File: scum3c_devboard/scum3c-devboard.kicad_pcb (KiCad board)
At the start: 2 copper layers, 142.2 x 96.5 mm, 59 parts, among them J1 47346-0001, J2 Conn_Coaxial, P3 Conn_01x02, P4 Conn_01x24, P5 Conn_01x02, U1 LP5907MFX-1.5, U10 LTC4123, U2 74AVC1T45GS,132, U3 FT231XS-U, U4 74AVC1T45GS,132, U5 74AVC4TD245PW,118, U6 74AVC4TD245PW,118, U7 ADT7302ARMZ, U8 scum3, U9AB1 MPU-9250

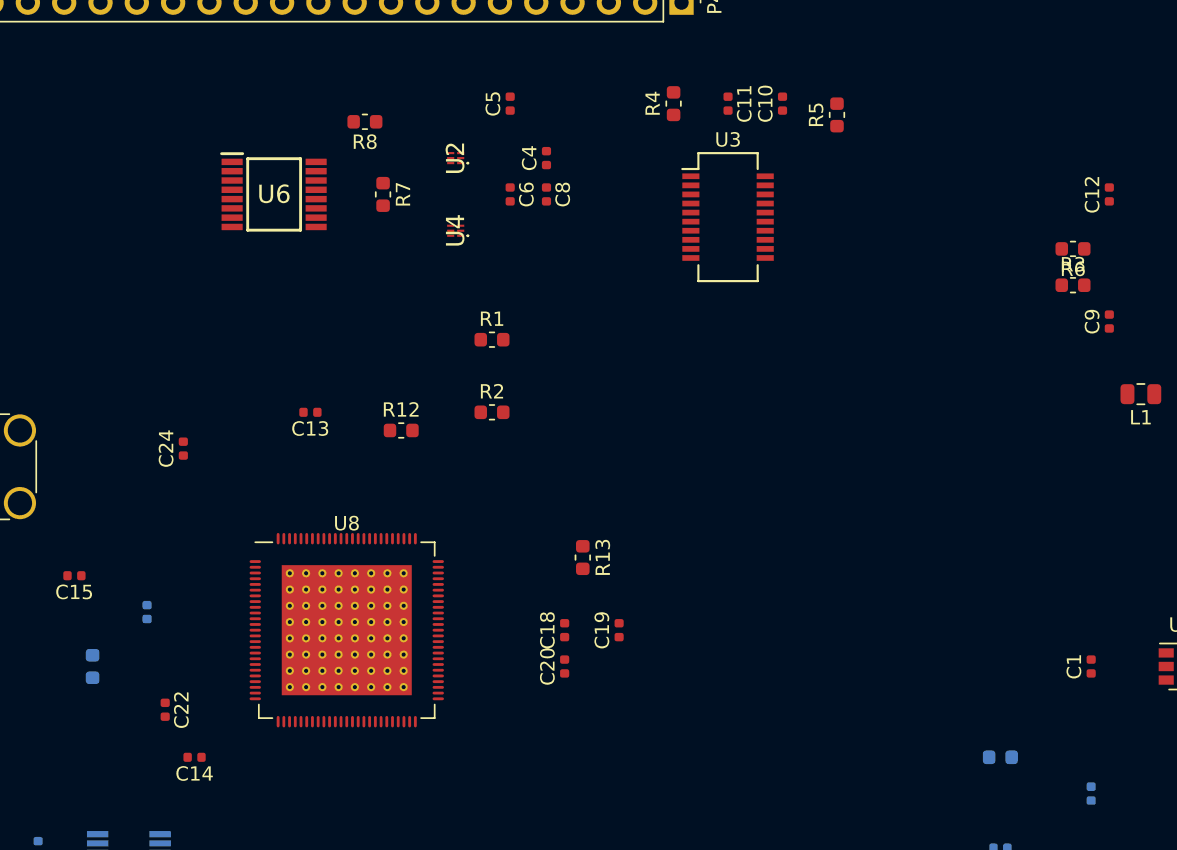
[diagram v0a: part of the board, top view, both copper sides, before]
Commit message: changed resistor smd footprint to 0402
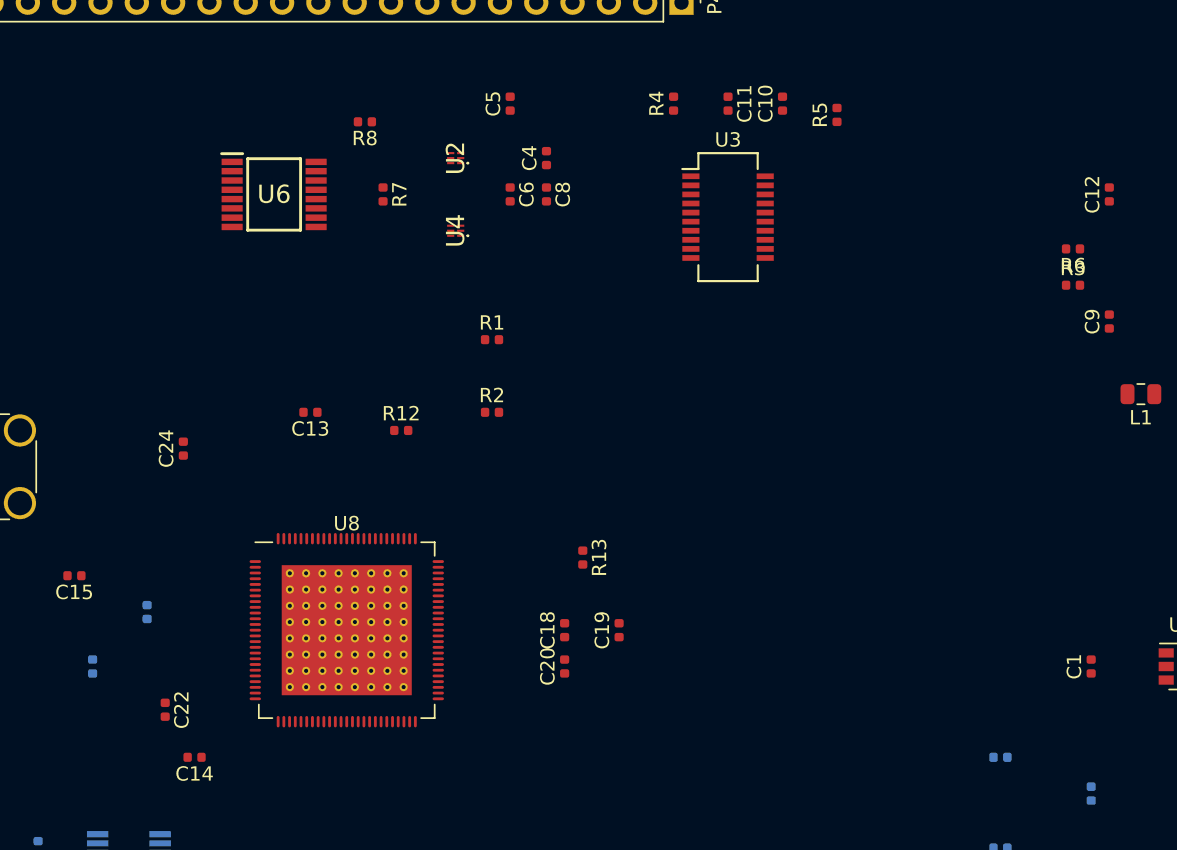
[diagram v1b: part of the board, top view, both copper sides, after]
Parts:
- R1, R12, R13, R14, R2, R3, R4, R5, R6, R7, R8, R9: footprint Resistor_SMD:R_0603_1608Metric -> Resistor_SMD:R_0402_1005Metric

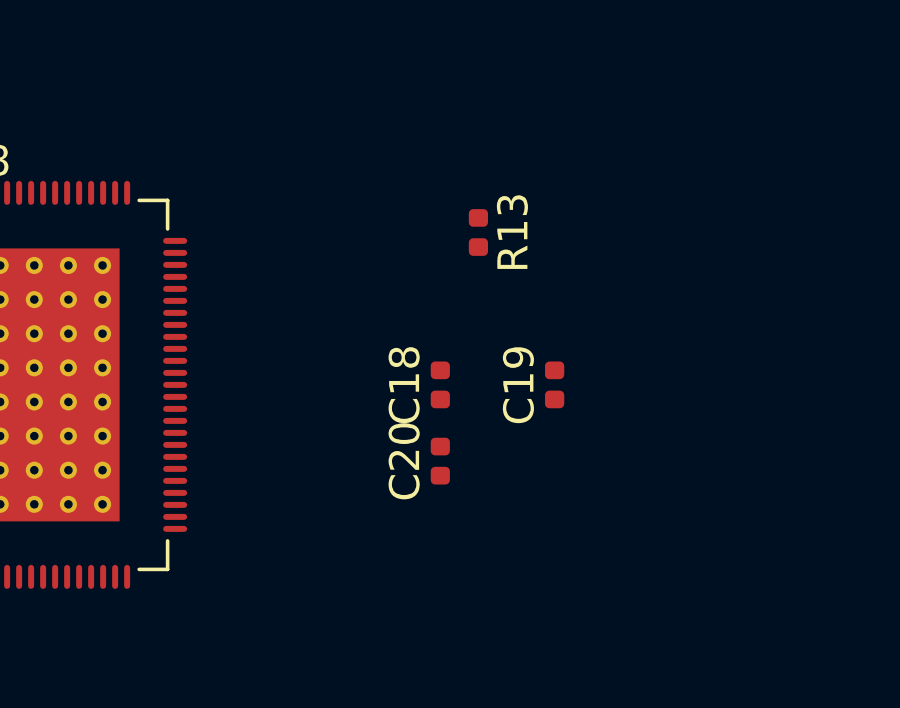
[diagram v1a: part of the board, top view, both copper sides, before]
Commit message: moved a resistor
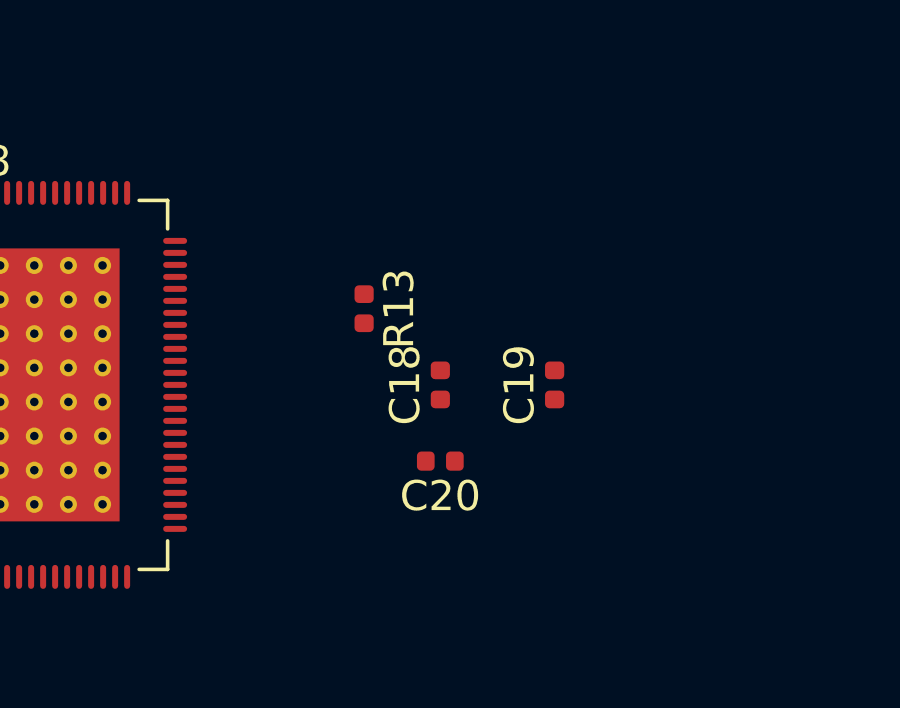
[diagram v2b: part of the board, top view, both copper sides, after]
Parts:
- moved R13 4.58 mm to (128.3, 90.2)
- turned C20 to 180 degrees
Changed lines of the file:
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@@
   )
   (module Resistor_SMD:R_0402_1005Metric (layer F.Cu)
-    (at 132.08 87.63 270)
+    (at 128.27 90.17 270)
     (descr "Resistor SMD 0402 (1005 Metric), square (rectangular) end terminal, IPC_7351 nominal, (Body size source: http://www.tortai-tech.com/upload/download/2011102023233369053.pdf), generated with kicad-footprint-generator")
     (tags resistor)
@@
   )
   (module Capacitor_SMD:C_0402_1005Metric (layer F.Cu)
-    (at 130.81 95.25 90)
-    (descr "Capacitor SMD 0402 (1005 Metric), square (rectangular) end terminal, IPC_7351 nominal, (Body size source: http://www.tortai-tech.com/upload/download/2011102023233369053.pdf), generated with kicad-footprint-generator")
-    (tags capacitor)
-    (attr smd)
-    (fp_text reference C20 (at 0 -1.17 90) (layer F.SilkS)
-      (effects (font (size 1 1) (thickness 0.15)))
-    )
-    (fp_text value NP (at 0 1.17 90) (layer F.Fab)
-      (effects (font (size 1 1) (thickness 0.15)))
-    )
-    (fp_line (start -0.5 0.25) (end -0.5 -0.25) (layer F.Fab) (width 0.1))
-    (fp_line (start -0.5 -0.25) (end 0.5 -0.25) (layer F.Fab) (width 0.1))
-    (fp_line (start 0.5 -0.25) (end 0.5 0.25) (layer F.Fab) (width 0.1))
-    (fp_line (start 0.5 0.25) (end -0.5 0.25) (layer F.Fab) (width 0.1))
-    (fp_line (start -0.93 0.47) (end -0.93 -0.47) (layer F.CrtYd) (width 0.05))
-    (fp_line (start -0.93 -0.47) (end 0.93 -0.47) (layer F.CrtYd) (width 0.05))
-    (fp_line (start 0.93 -0.47) (end 0.93 0.47) (layer F.CrtYd) (width 0.05))
-    (fp_line (start 0.93 0.47) (end -0.93 0.47) (layer F.CrtYd) (width 0.05))
-    (fp_text user %R (at 0 0 90) (layer F.Fab)
-      (effects (font (size 0.25 0.25) (thickness 0.04)))
-    )
-    (pad 1 smd roundrect (at -0.485 0 90) (size 0.59 0.64) (layers F.Cu F.Paste F.Mask) (roundrect_rratio 0.25)
-      (net 2 GND))
-    (pad 2 smd roundrect (at 0.485 0 90) (size 0.59 0.64) (layers F.Cu F.Paste F.Mask) (roundrect_rratio 0.25)
+    (at 130.81 95.25 180)
+    (descr "Capacitor SMD 0402 (1005 Metric), square (rectangular) end terminal, IPC_7351 nominal, (Body size source: http://www.tortai-tech.com/upload/download/2011102023233369053.pdf), generated with kicad-footprint-generator")
+    (tags capacitor)
+    (attr smd)
+    (fp_text reference C20 (at 0 -1.17) (layer F.SilkS)
+      (effects (font (size 1 1) (thickness 0.15)))
+    )
+    (fp_text value NP (at 0 1.17) (layer F.Fab)
+      (effects (font (size 1 1) (thickness 0.15)))
+    )
+    (fp_line (start -0.5 0.25) (end -0.5 -0.25) (layer F.Fab) (width 0.1))
+    (fp_line (start -0.5 -0.25) (end 0.5 -0.25) (layer F.Fab) (width 0.1))
+    (fp_line (start 0.5 -0.25) (end 0.5 0.25) (layer F.Fab) (width 0.1))
+    (fp_line (start 0.5 0.25) (end -0.5 0.25) (layer F.Fab) (width 0.1))
+    (fp_line (start -0.93 0.47) (end -0.93 -0.47) (layer F.CrtYd) (width 0.05))
+    (fp_line (start -0.93 -0.47) (end 0.93 -0.47) (layer F.CrtYd) (width 0.05))
+    (fp_line (start 0.93 -0.47) (end 0.93 0.47) (layer F.CrtYd) (width 0.05))
+    (fp_line (start 0.93 0.47) (end -0.93 0.47) (layer F.CrtYd) (width 0.05))
+    (fp_text user %R (at 0 0) (layer F.Fab)
+      (effects (font (size 0.25 0.25) (thickness 0.04)))
+    )
+    (pad 1 smd roundrect (at -0.485 0 180) (size 0.59 0.64) (layers F.Cu F.Paste F.Mask) (roundrect_rratio 0.25)
+      (net 2 GND))
+    (pad 2 smd roundrect (at 0.485 0 180) (size 0.59 0.64) (layers F.Cu F.Paste F.Mask) (roundrect_rratio 0.25)
       (net 15 /scumsheet/AUX_LDO_OUTPUT))
     (model ${KISYS3DMOD}/Capacitor_SMD.3dshapes/C_0402_1005Metric.wrl

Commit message: made up some design rules
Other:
- net class smaller: clearance 0.05 -> 0.2; via_dia 0.4 -> 0.6
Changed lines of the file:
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@@
   (setup
     (last_trace_width 0.25)
+    (user_trace_width 0.2)
     (trace_clearance 0.2)
     (zone_clearance 0.508)
@@
     (via_min_size 0.4)
     (via_min_drill 0.3)
+    (user_via 0.6 0.3)
     (uvia_size 0.3)
     (uvia_drill 0.1)
@@
     (via_drill 0.4)
     (uvia_dia 0.3)
+    (uvia_drill 0.1)
+  )
+  (net_class smaller ""
+    (clearance 0.2)
+    (trace_width 0.2)
+    (via_dia 0.6)
+    (via_drill 0.3)
+    (uvia_dia 0.2)
     (uvia_drill 0.1)
     (add_net +UART33)
@@
     (add_net "Net-(U9AB1-Pad9)")
   )
-  (net_class smaller ""
-    (clearance 0.05)
-    (trace_width 0.2)
-    (via_dia 0.4)
-    (via_drill 0.3)
-    (uvia_dia 0.2)
-    (uvia_drill 0.1)
-    (diff_pair_width 0.2)
-    (diff_pair_gap 0.05)
-  )
   (module Resistor_SMD:R_0402_1005Metric (layer B.Cu)
